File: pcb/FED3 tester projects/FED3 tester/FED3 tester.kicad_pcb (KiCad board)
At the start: 4 copper layers, 108 x 134.4 mm, 164 parts, among them J1 USB4105-GF-A, J2 Conn_02x03_Odd_Even, J3 6pin_hd, J4 Conn_02x03_Odd_Even, J5 MotorCkeck1, J6 MotorCkeck2, J7 Conn_01x02_Socket, K1 Relay SPDT, K2 Relay SPDT, K3 Relay SPDT, Q1 DMN63D8L-7, Q2 PMF170XP,115, Q3 DMN63D8L-7, Q4 DMN63D8L-7, Q5 DMN63D8L-7, Q6 DMN63D8L-7, SW1 SW_SPST, SW2 SW_SPST, SW3 SW_SPST, SW4 SW_SPST, SW5 SW_SPST, SW6 SW_SPST, SW7 SW_SPST, SW8 SW_SPST, SW9 SW_SPST, U1 FT232RL, U2 LP5907MFX-3.3, U3 LP5907MFX-3.3, U4 TPS73801DCQR, U5 ATXMEGA32A4U-MH, U6 THS4281, U7 THS4281, U8 THS4281, U9 ZXCT1082

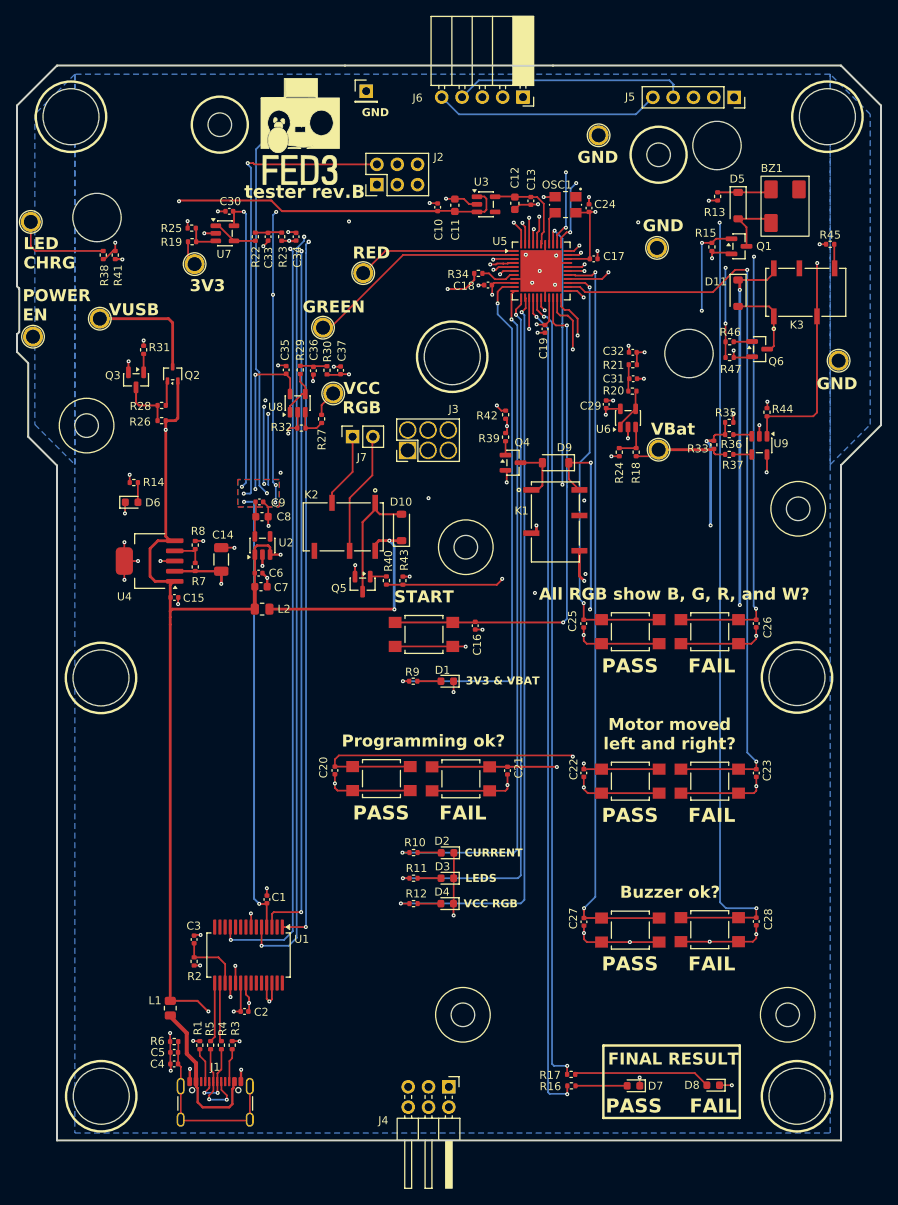
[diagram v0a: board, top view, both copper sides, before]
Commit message: adicionadas stitching-vias a planos GND
nota:
- não tem plano GND no top-layer, pq o attach-to-pads é sempre feito a 0.5mm independentemente do setup q se faça no plano;
(algo já reportado com Kicad-bug em v10.0)
- haveria situações em q entrava em conflito com pitch de componentes; tamanho de pads etc
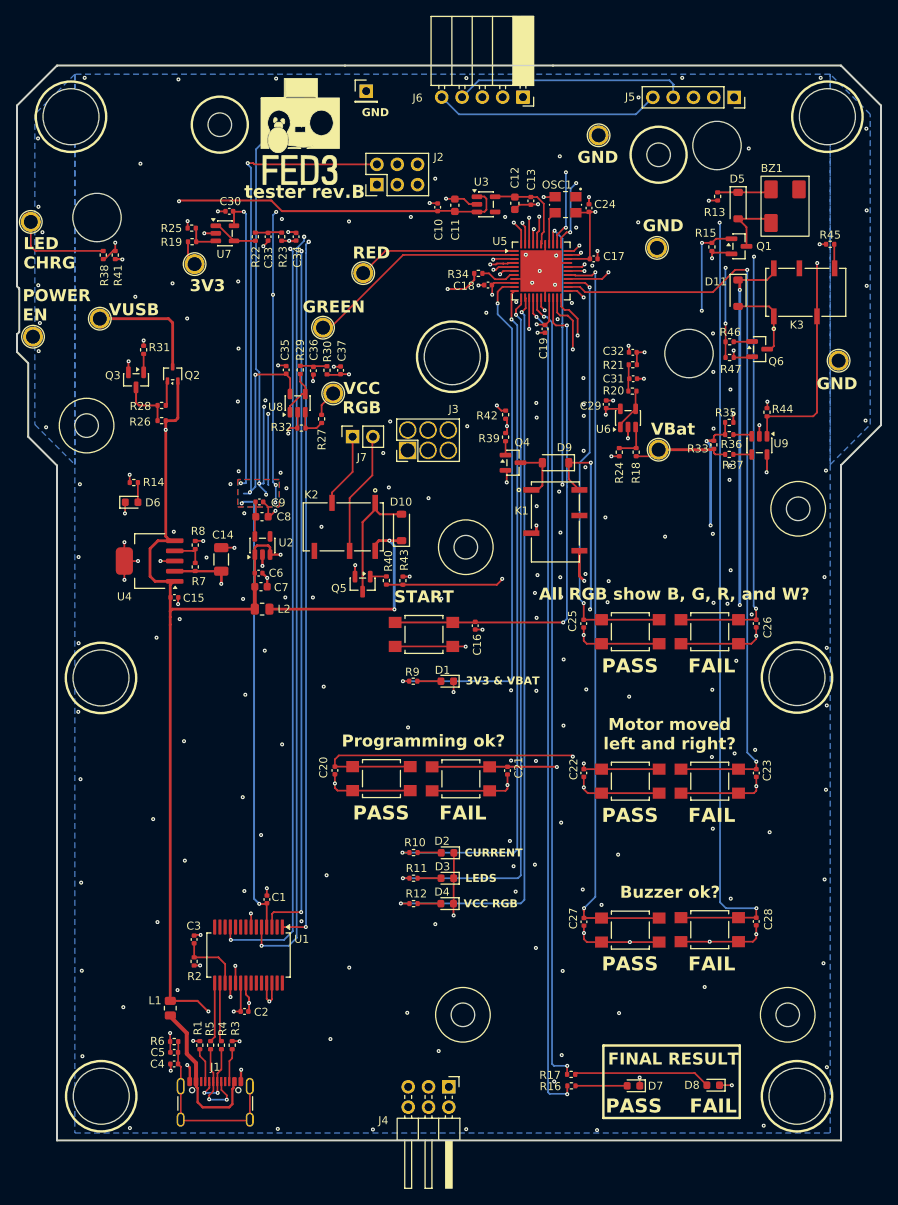
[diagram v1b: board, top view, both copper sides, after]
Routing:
- net GND: track 217.1 -> 218.9 mm, vias 82 -> 237
- net +3V3: track 595.8 -> 597.4 mm, vias 23 -> 22

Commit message: State LED - modificada côr para amarelo
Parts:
- D6: value Red -> Yellow
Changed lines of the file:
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@@
 			)
 		)
-		(property "Value" "Red"
+		(property "Value" "Yellow"
 			(at 0 1.43 0)
 			(unlocked yes)
@@
 			)
 		)
-		(property "Description" "LED 0603 Red 635nm 20mA"
+		(property "Description" "LED 0603 Yellow 590nm 20mA"
 			(at 0 0 0)
 			(unlocked yes)
@@
 			)
 		)
-		(property "MPN" "VFHR1116P-4C82A-TR"
+		(property "MPN" "5990040007F"
 			(at 0 0 0)
 			(unlocked yes)
@@
 			)
 		)
-		(property "OEPSPN" "OEPS030038"
+		(property "OEPSPN" "OEPS030043"
 			(at 0 0 0)
 			(unlocked yes)

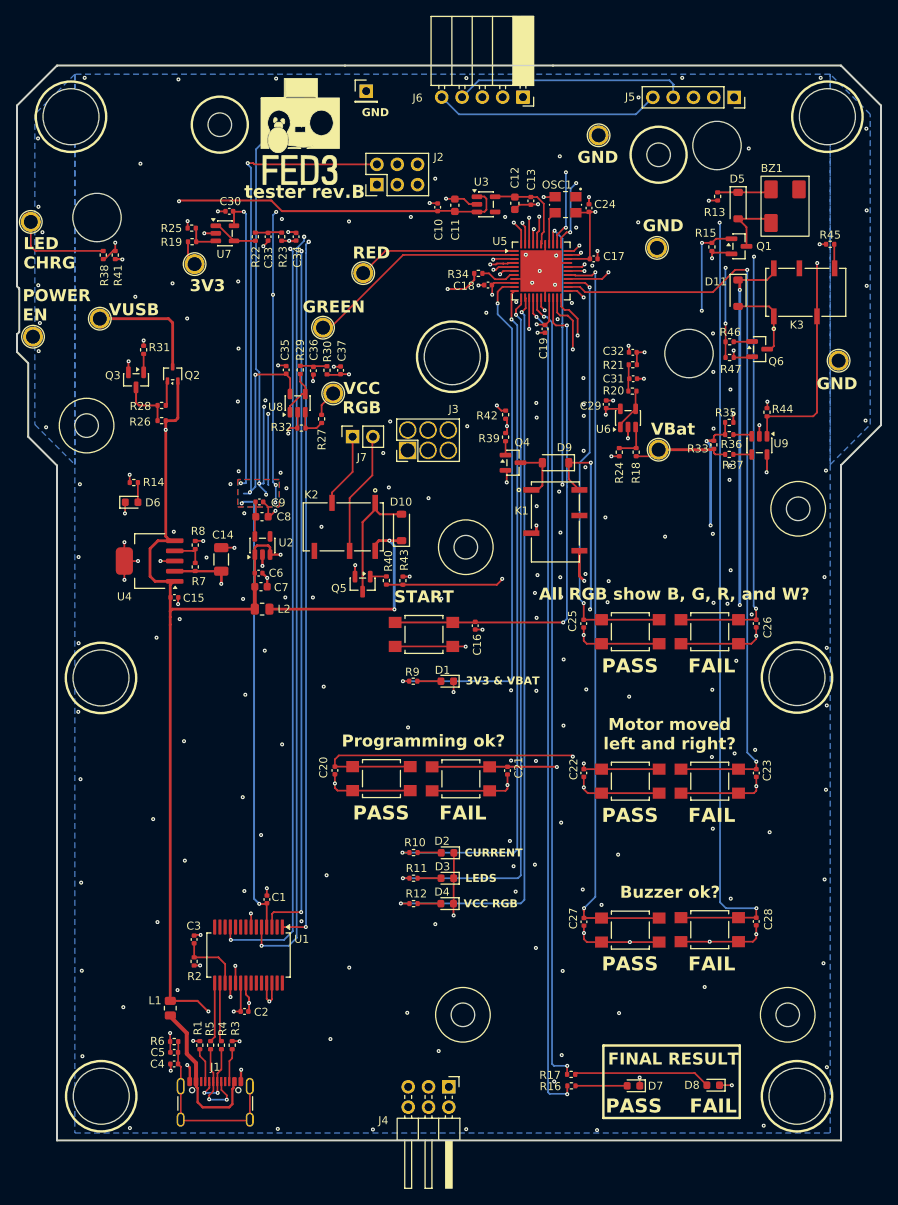
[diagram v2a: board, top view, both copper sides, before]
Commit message: completos OEPSPN & MPN
- andar de I-measure  ZXCT1086 redimensionado
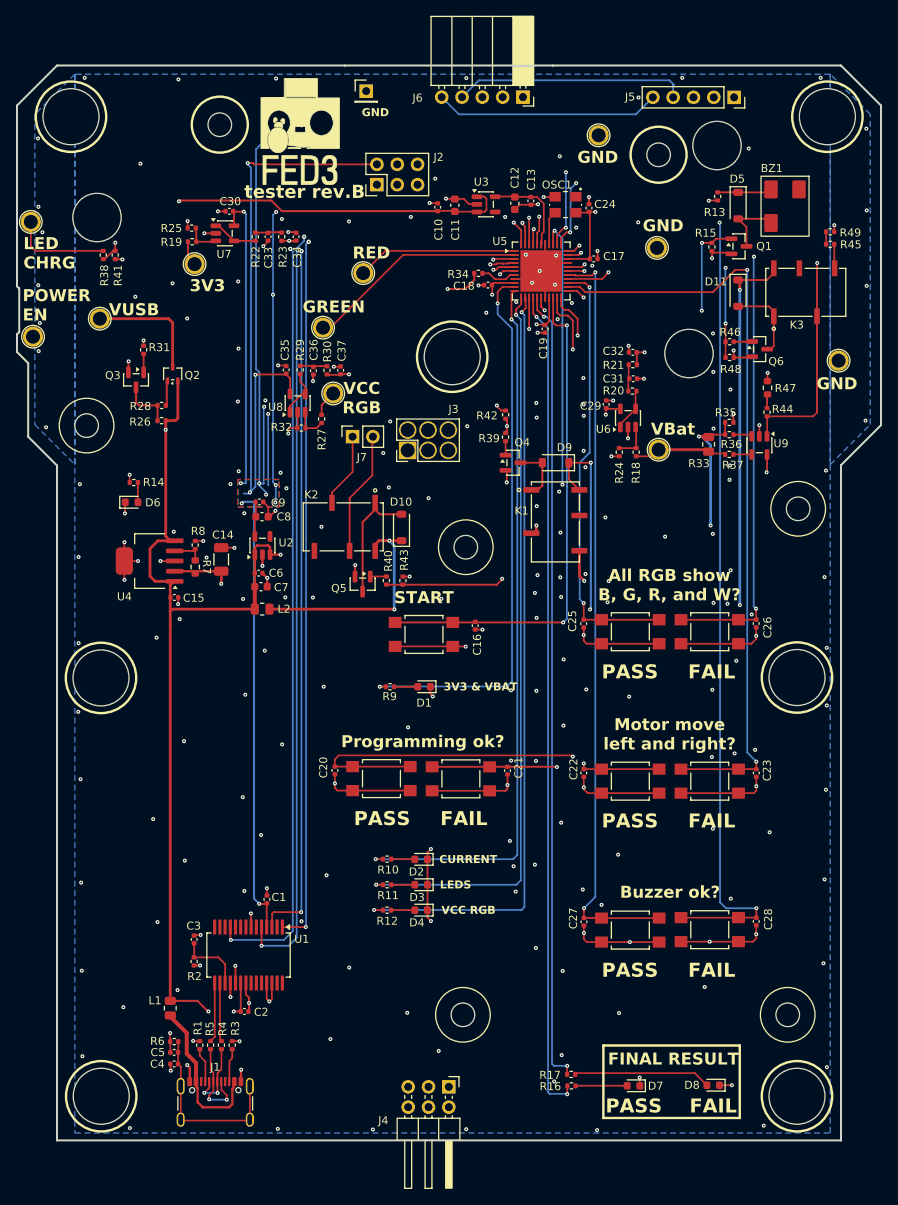
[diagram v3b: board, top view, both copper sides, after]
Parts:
- added R47: 4k3, Resistor_SMD:R_0603_1608Metric, F.Cu at (150.5, 64.4)
- added R49: 249k, Resistor_SMD:R_0402_1005Metric, F.Cu at (158.4, 44.9)
- R26, R31: value 1.2K -> 1.2k
- R28: value 1.2K ?? -> 1.2k
- R33: value 10R -> 0.5R; footprint Resistor_SMD:R_0402_1005Metric -> Resistor_SMD:R_0805_2012Metric
- R36, R37: value 1.2K -> 5k
- R38: value 640k -> 649k
- R44: value 2M -> 24k
- R45: value 22k -> 249k
- R7: footprint Resistor_SMD:R_0402_1005Metric -> Resistor_SMD:R_0603_1608Metric
- R8: value 4k -> 3.3k
- moved D2 3.40 mm to (107.2, 123.4)
- moved R10 3.40 mm to (103.0, 123.4)
- moved R11 3.40 mm to (103.0, 126.6)
- moved R12 3.40 mm to (103.0, 129.7)
- moved D3 3.38 mm to (107.2, 126.6)
- moved D4 3.35 mm to (107.2, 129.7)
- moved D1 2.98 mm to (107.6, 101.8)
- moved R9 2.98 mm to (103.3, 101.8)
- moved R33 0.66 mm to (143.2, 71.5)
- renumbered R47 to R48
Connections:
- R44 pad 2: GND -> Net-(R44-Pad2)
- R45 pad 1: GND -> Net-(R45-Pad1)
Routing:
- net /main core/LED#4: track 92.4 -> 96.6 mm
- net /main core/LED#2: track 85.7 -> 89.7 mm
- net /main core/LED#3: track 88.5 -> 92.5 mm
- net /main core/LED#1: track 66.0 -> 69.4 mm
- net Net-(R44-Pad2): track 0.00 -> 1.82 mm
- net GND: track 218.9 -> 220.7 mm
- net Net-(R45-Pad1): track 0.00 -> 1.56 mm
- net Net-(K1-Pad3): track 38.0 -> 38.9 mm
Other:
- board text added: "Motor move left and right?"
- board text removed: "Motor moved left and right?"
